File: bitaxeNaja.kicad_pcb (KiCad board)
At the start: 6 copper layers, 65 x 112 mm, 199 parts, among them J1 XT30, J2 Conn_01x08, J3 Conn_01x04, J4 USB_C_Receptacle_USB2.0, J7 Conn_01x04, SW1 SWITCH-SPST, SW2 SWITCH-SPST, U1 STHW4-DU-HN050206, U10 TLV77308PDBVR, U11 TLV77312PDBVR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

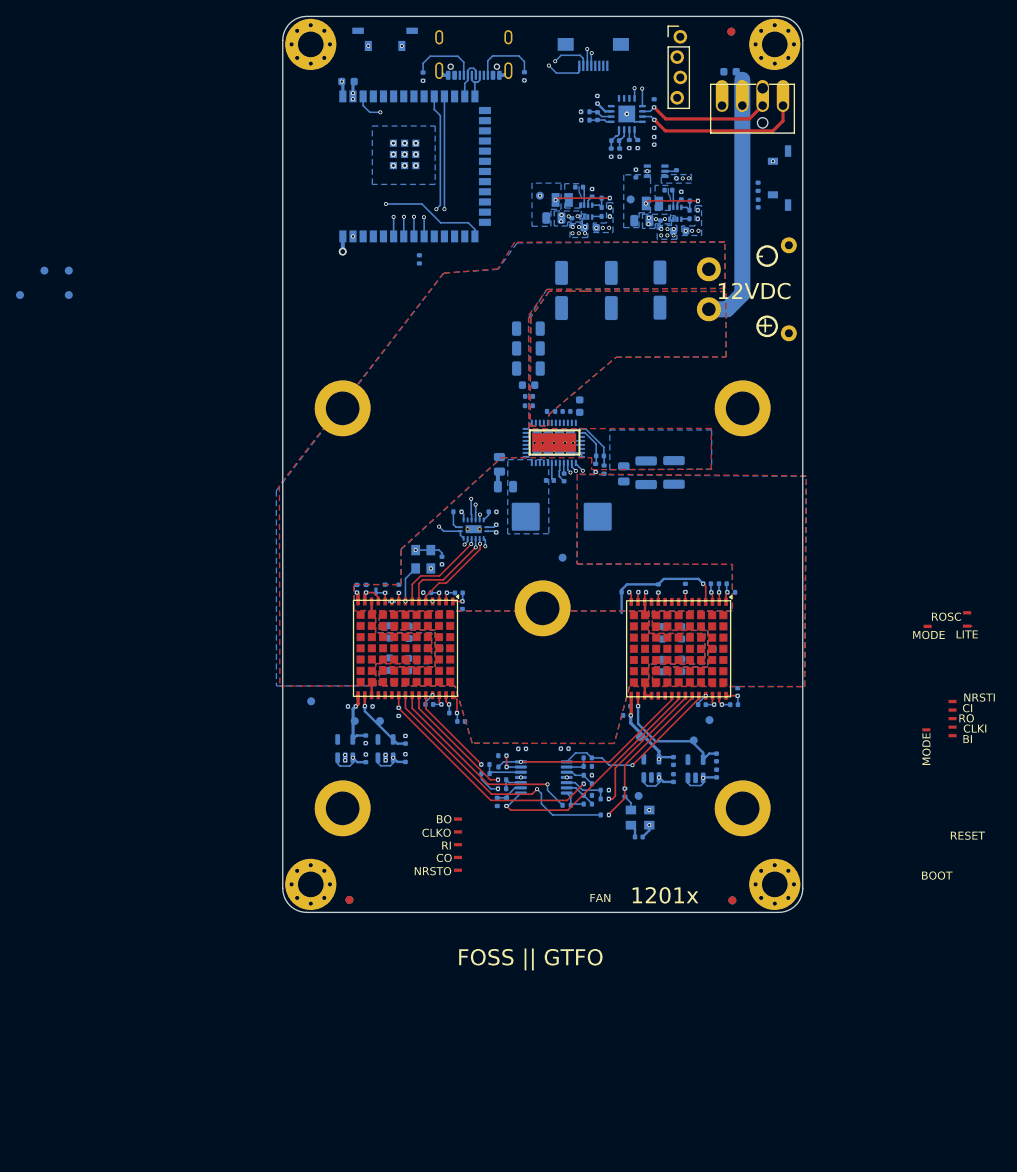
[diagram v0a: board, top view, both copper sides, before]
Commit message: add missing 3d models
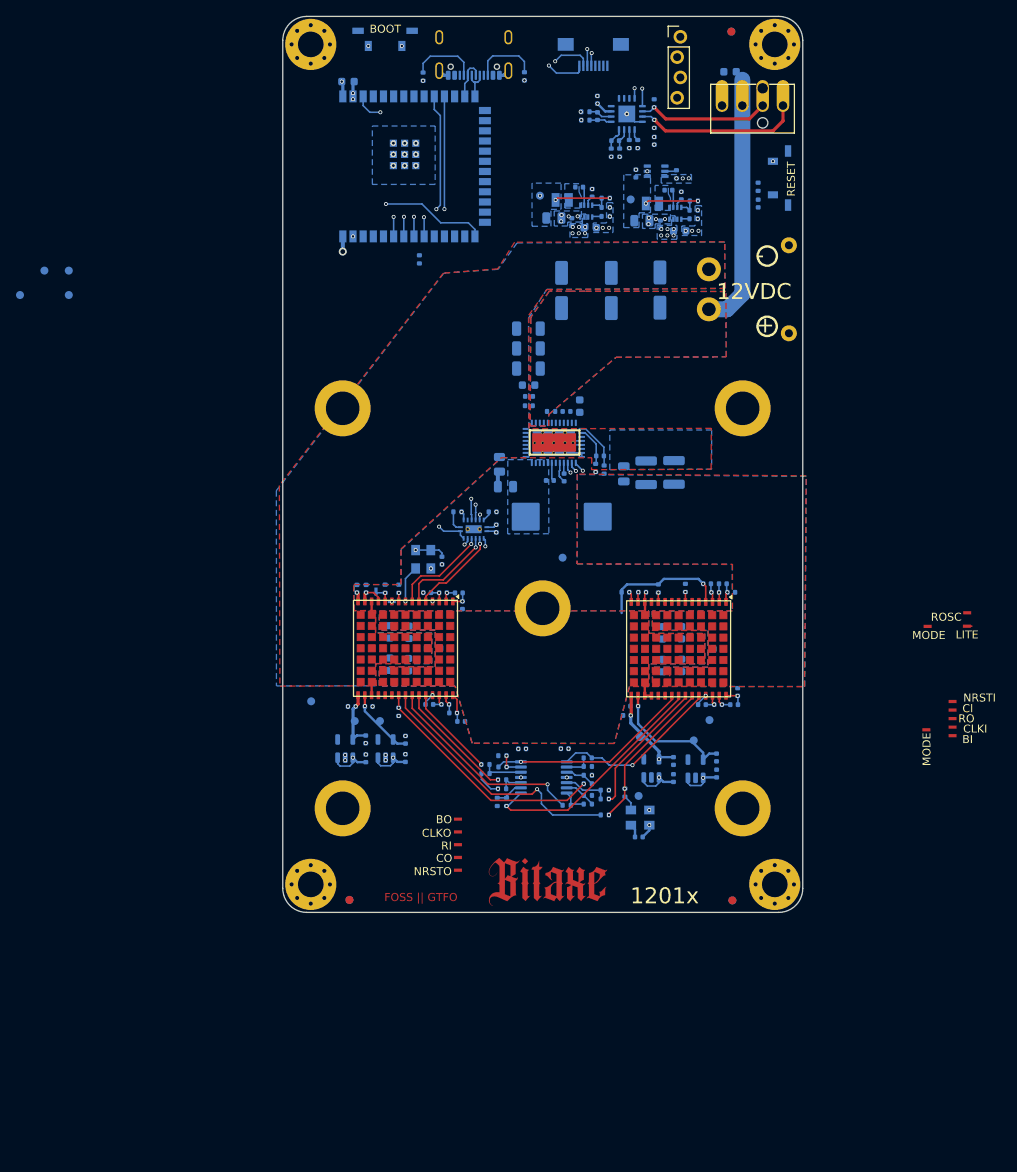
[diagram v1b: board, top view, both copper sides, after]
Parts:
- removed the G*** at (151.4, 174.8)
- added G***: LOGO, bitaxe:bitaxe_logo_small, F.Cu at (131.7, 146.2)
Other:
- board text removed: "FAN"

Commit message: finished routing
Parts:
- removed NT1: NetTie_2, bitaxe:NetTie-2_SMD_Pad0.2mmx1mm
- TP11, TP13, TP17, TP18, TP19, TP22, TP23, TP41, TP42, TP5, TP6, TP7, TP8, TP9: moved to B.Cu
- moved TP16 87.5 mm to (149.2, 103.9)
- moved TP41 69.2 mm to (110.5, 122.9), turned to -90 degrees
- moved TP21 68.2 mm to (139.1, 58.7)
- moved TP1 64.8 mm to (126.8, 51.3)
- moved TP20 47.3 mm to (107.3, 103.9)
- moved TP9 42.6 mm to (140.2, 130.4)
- moved TP8 40.2 mm to (142.3, 129.1)
- moved TP13 38.7 mm to (145.4, 110.9)
- moved TP7 37.0 mm to (145.3, 127.1)
- moved TP6 36.9 mm to (145.4, 128.1)
- moved TP11 36.7 mm to (147.4, 110.1)
- moved TP5 36.5 mm to (145.7, 129.2)
- moved TP42 35.1 mm to (144.2, 122.9)
- moved TP4 19.1 mm to (114.7, 108.9)
- moved R3 18.0 mm to (126.0, 53.6), turned to 180 degrees
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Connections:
- C10 pad 1: /Power/AGND -> GND
- R29 pad 2: /ASIC/TEMP2_P -> /ASIC/TEMP1_P
- R32 pad 2: /ASIC/TEMP2_N -> /ASIC/TEMP1_N
- R34 pad 2: /ASIC/TEMP1_P -> /ASIC/TEMP2_P
- R36 pad 2: /ASIC/TEMP1_N -> /ASIC/TEMP2_N
- U3 pad 29: /Power/AGND -> GND
- U3 pad 37: /Power/AGND -> GND
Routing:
- net /ASIC/TEMP1_P: track 0.00 -> 104.3 mm, vias 1 -> 2
- net /ASIC/TEMP1_N: track 0.00 -> 104.0 mm, vias 1 -> 2
- net /ASIC/TEMP2_N: track 0.00 -> 99.5 mm, vias 1 -> 2
- net /ASIC/TEMP2_P: track 0.00 -> 98.1 mm, vias 1 -> 2
- net /ASIC/GND_1: track 25.0 -> 92.8 mm, vias 3 -> 134
- net /3V3: track 86.4 -> 145.5 mm, vias 7 -> 14
- net /Power/PGOOD: track 1.35 -> 51.3 mm, vias 1 -> 2
- net /ESP32/SMB_ALRT: track 0.01 -> 48.8 mm, vias 0 -> 2
- net /ESP32/PWR_EN: track 0.00 -> 45.9 mm, vias 0 -> 2
- net /ESP32/SCL: track 39.9 -> 80.7 mm, vias 2 -> 3
- net /ESP32/SDA: track 39.5 -> 78.0 mm, vias 2 -> 3
- net /ESP32/EN: track 20.1 -> 58.0 mm, vias 1 -> 2
- net /12V: track 31.8 -> 67.4 mm, vias 12 -> 121
- net /ESP32/5V_EN: track 0.00 -> 23.5 mm
- net GND: track 27.4 -> 35.8 mm, vias 67 -> 480
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- added copper zone on In2.Cu, net /ASIC/GND_1
- added copper zone on F.Cu, net /Power/SW1
- added copper zone on In2.Cu, net /Power/SW1

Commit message: DRC pass
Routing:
- net /ASIC/TEMP2_P: track 98.1 -> 95.8 mm
- net /ASIC/TEMP2_N: track 99.5 -> 97.3 mm
- net GND: vias 480 -> 486
- net /VDD: vias 147 -> 157

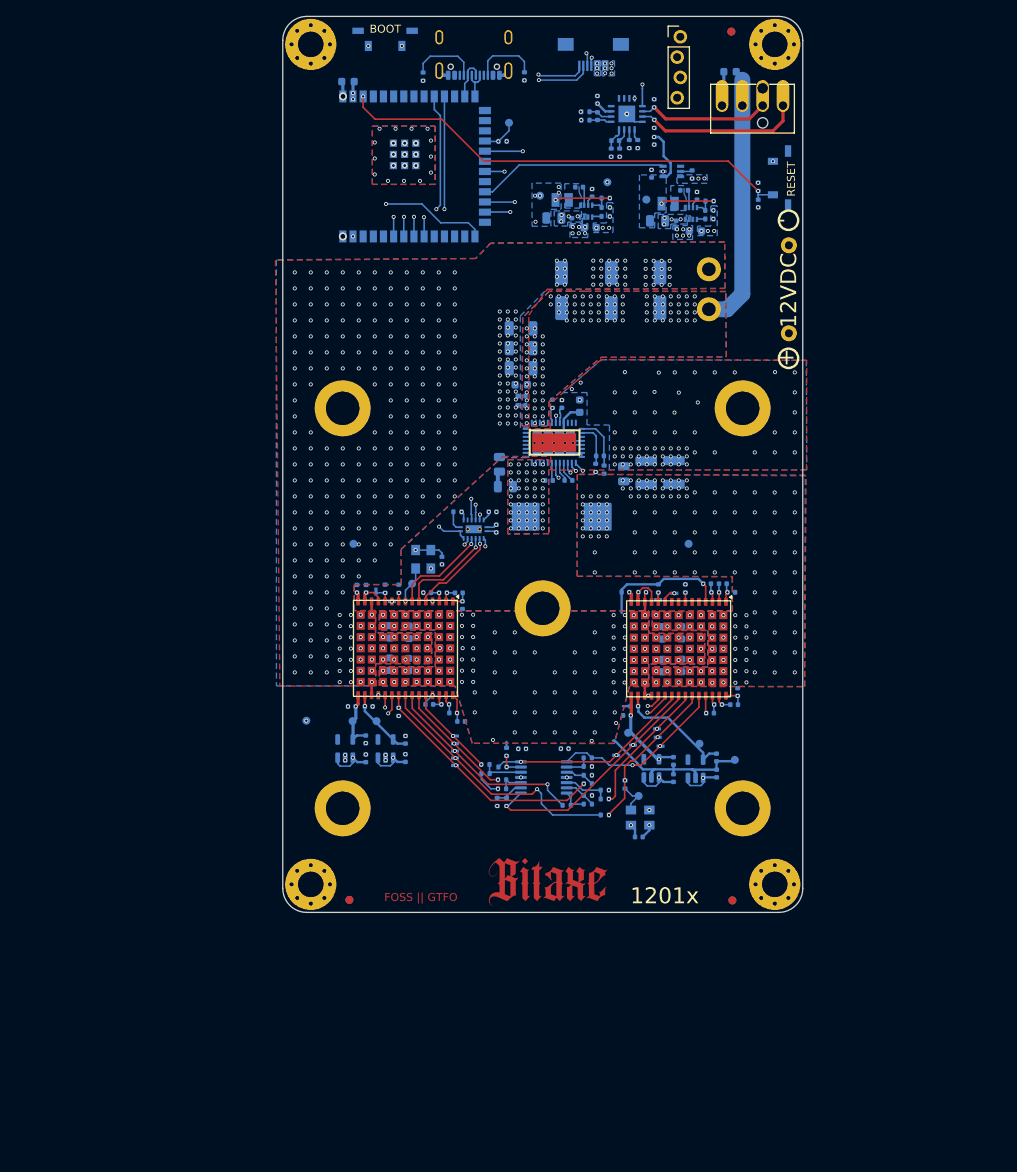
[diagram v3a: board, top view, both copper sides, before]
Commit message: make the PCB bigger for 70mm heatsink mounting holes
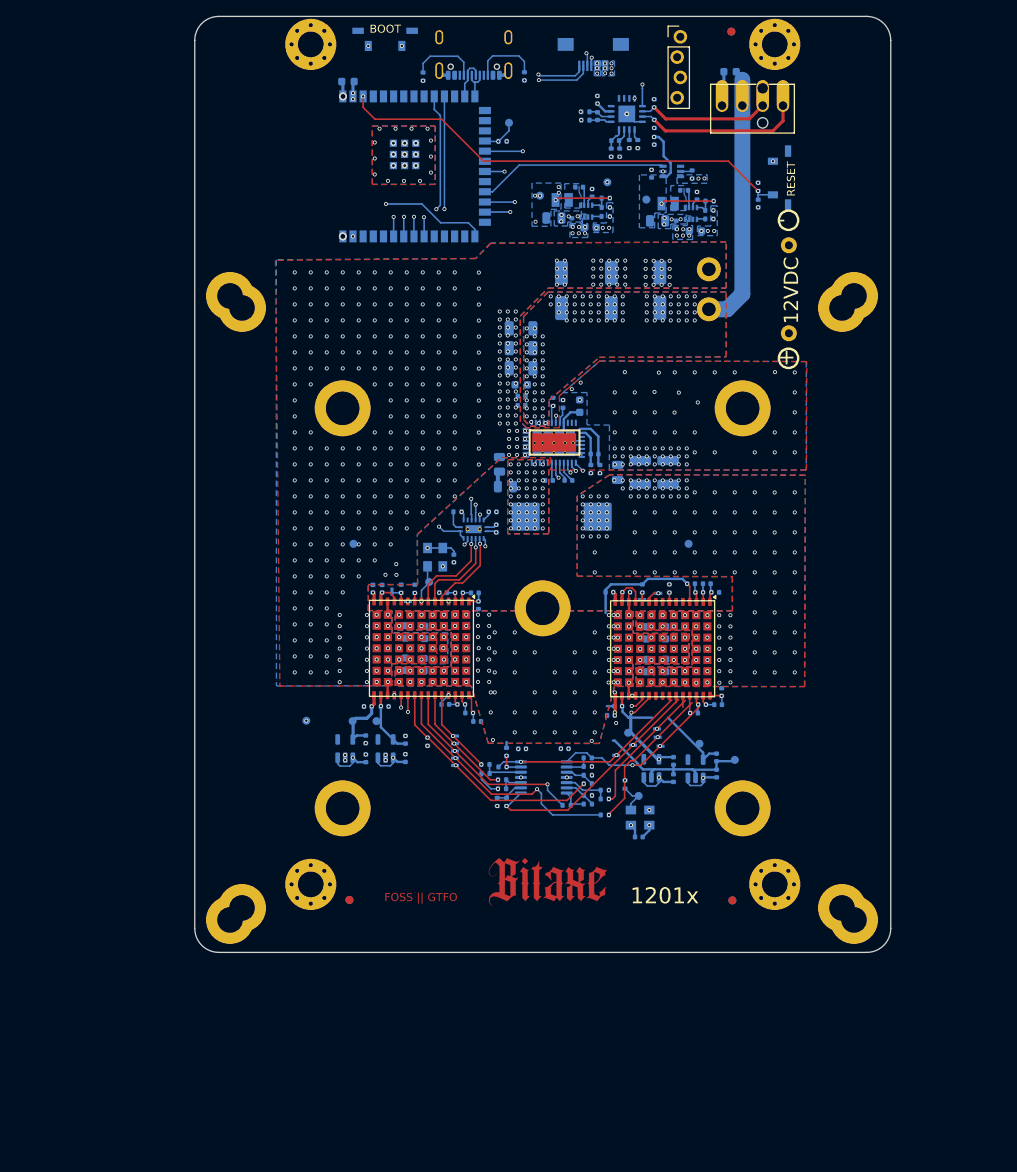
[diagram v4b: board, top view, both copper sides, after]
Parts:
- added HS2: Heatsink, bitaxe:70mm-mounting_HTPC, F.Cu at (130.9, 112.0)
- moved R27 5.19 mm to (116.6, 128.7)
- moved TP4 2.14 mm to (116.8, 108.7)
- moved A1 2.00 mm to (115.8, 117.0)
- moved A2 2.00 mm to (146.0, 117.0)
- moved C58 2.00 mm to (144.0, 119.2)
- moved C59 2.00 mm to (146.3, 119.1)
- moved C60 2.00 mm to (149.5, 117.1)
- moved C61 2.00 mm to (146.3, 115.0)
- moved C62 2.00 mm to (143.9, 115.1)
- moved C64 2.00 mm to (118.5, 110.0)
- moved C65 2.00 mm to (120.5, 110.0)
- moved C66 2.00 mm to (122.5, 110.1)
- moved C67 2.00 mm to (123.0, 111.6)
- moved C68 2.00 mm to (122.8, 126.1)
- moved C69 2.00 mm to (121.8, 125.1)
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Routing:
- net GND: track 35.8 -> 83.5 mm, vias 486 -> 514
- net /VDD: track 0.09 -> 24.8 mm, vias 157 -> 159
- net /ASIC/TEMP1_N: track 104.0 -> 100.6 mm
- net /ASIC/1V2_0: track 39.2 -> 40.9 mm
- net /ASIC/TEMP1_P: track 104.3 -> 103.2 mm
- net /ASIC/RST_1V2: track 11.2 -> 10.4 mm
- net /ASIC/TX_1V2: track 12.3 -> 11.5 mm
- net /ASIC/Level Shifter/RO: track 25.9 -> 25.1 mm
- net /ASIC/Level Shifter/CI: track 15.2 -> 14.4 mm
- net /ASIC/0V8_0: track 12.2 -> 11.4 mm
- net /ASIC/Level Shifter/NRSTI: track 11.5 -> 10.7 mm
- net /ASIC/Level Shifter/CLKI: track 32.8 -> 32.0 mm
- net /ASIC/Level Shifter/BI: track 30.4 -> 29.6 mm
- net /ASIC/RX_1V2: track 12.3 -> 11.6 mm
- net Net-(U3-GOSNS): track 5.48 -> 4.77 mm
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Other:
- board size 65 x 112 mm -> 87 x 117 mm
